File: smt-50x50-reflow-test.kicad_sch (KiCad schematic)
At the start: 104 parts, among them J1 Conn_01x04_Pin, J2 Conn_01x02, J3 Conn_01x01, J4 USB_C_Receptacle_USB2.0_14P, J5 Conn_01x01, J6 Conn_01x01, J7 Conn_01x01, J8 Conn_01x04_Pin, J9 Conn_01x03_Pin, SW1 SW_Push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

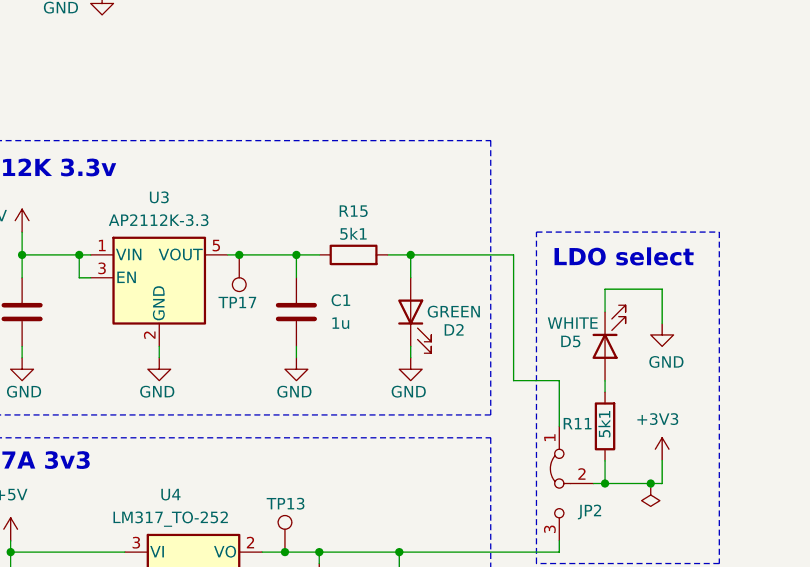
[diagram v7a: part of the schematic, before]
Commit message: pcb: add power section routing
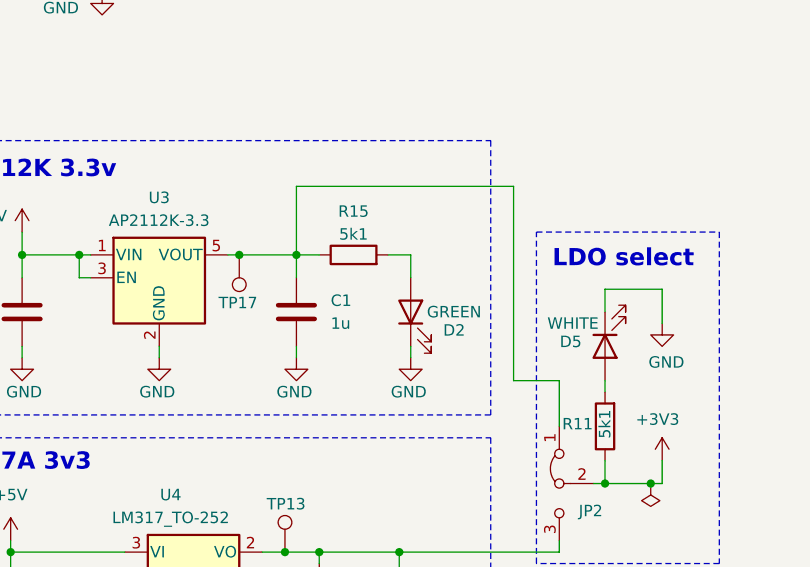
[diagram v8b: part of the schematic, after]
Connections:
- net at C1.1, R15.1, TP17.1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: now also JP2.1 (A)
- net at D2.2 (A), R15.2: no longer JP2.1 (A)
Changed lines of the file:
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@@
-	)
-	(junction
-		(at 139.7 142.24)
-		(diameter 0)
-		(color 0 0 0 0)
 	)
 	(junction
@@
 	(wire
 		(pts
+			(xy 151.13 134.62) (xy 127 134.62)
+		)
+		(stroke
+			(width 0)
+			(type default)
+		)
+	)
+	(wire
+		(pts
 			(xy 69.85 33.02) (xy 59.69 33.02)
 		)
@@
 	(wire
 		(pts
-			(xy 151.13 156.21) (xy 151.13 142.24)
+			(xy 151.13 134.62) (xy 151.13 156.21)
 		)
 		(stroke
@@
 	(wire
 		(pts
-			(xy 151.13 142.24) (xy 139.7 142.24)
-		)
-		(stroke
-			(width 0)
-			(type default)
-		)
-	)
-	(wire
-		(pts
 			(xy 129.54 176.53) (xy 129.54 175.26)
 		)
@@
 		)
 		(stroke
+			(width 0)
+			(type default)
+		)
+	)
+	(wire
+		(pts
+			(xy 127 134.62) (xy 127 142.24)
+		)
+		(stroke
